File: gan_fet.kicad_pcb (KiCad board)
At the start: 2 copper layers, 10.2 x 22 mm, 7 parts, among them J1 Conn_01x04_Male, Q1 EPC2036, U1 NPC81074

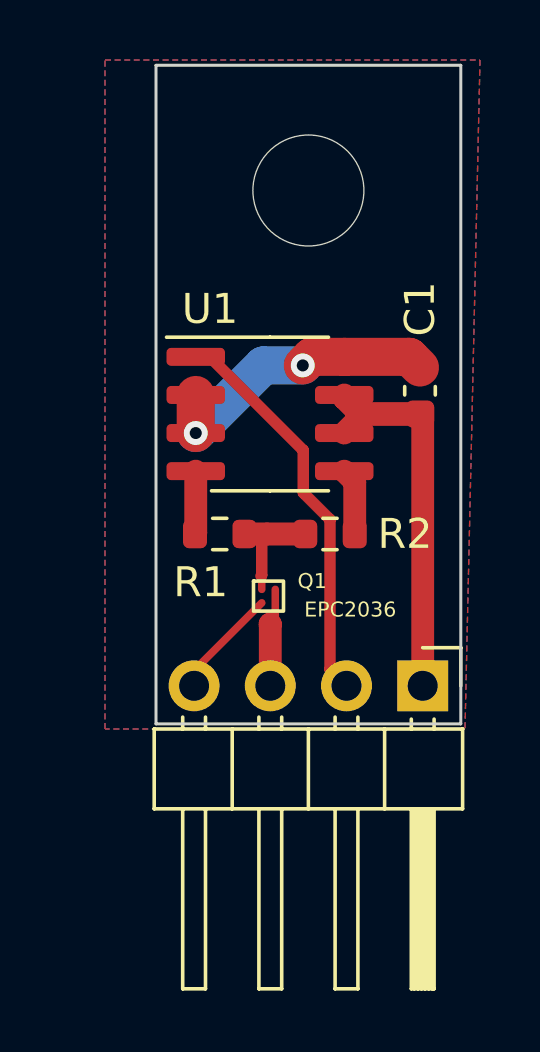
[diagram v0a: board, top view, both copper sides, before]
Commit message: Increased trace width for mosfet drain and source
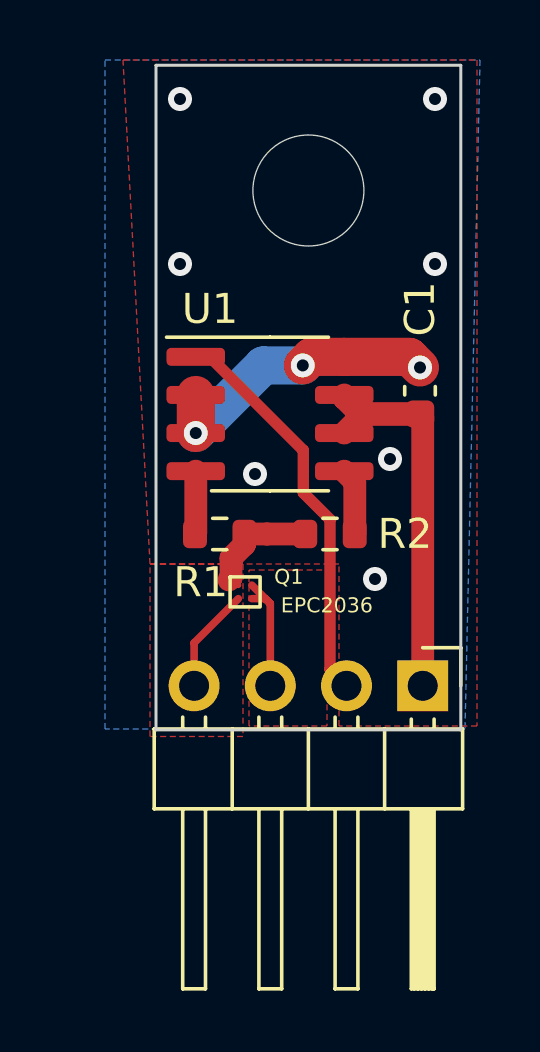
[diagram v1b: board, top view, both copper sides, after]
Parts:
- moved Q1 0.79 mm to (142.2, 96.4)
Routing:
- net /drain: track 3.29 -> 4.29 mm
- net GND: track 13.6 -> 13.5 mm, vias 2 -> 10
- added copper zone on F.Cu, net /drain
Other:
- board size 10.2 x 22 mm -> 10.2 x 22.2 mm
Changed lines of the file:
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@@
   )
   (footprint "epc:epc2036" (layer "F.Cu")
-    (at 143 96.52 90)
+    (at 142.22 96.38 90)
     (property "Sheetfile" "gan_fet.kicad_sch")
     (property "Sheetname" "")
@@
     )
   )
-  (gr_rect (start 149.86 78.375) (end 139.7 100.33) (layer "Edge.Cuts") (width 0.1) (fill none))
+  (gr_rect (start 149.86 78.375) (end 139.7 100.53) (layer "Edge.Cuts") (width 0.1) (fill none))
   (gr_text "+5 G D S" (at 144.999989 97.000009) (layer "B.SilkS")
     (effects (font (size 1.27 1.27) (thickness 0.15)) (justify mirror))
@@
   (segment (start 148.5 90) (end 146.5 90) (width 0.762) (layer "F.Cu") (net 1))
   (segment (start 145.975 89.475) (end 145.975 89.365) (width 0.762) (layer "F.Cu") (net 1))
+  (segment (start 142.445 96.155) (end 140.97 97.63) (width 0.254) (layer "F.Cu") (net 2))
   (segment (start 145.975 88.095) (end 144.877679 88.095) (width 1.27) (layer "F.Cu") (net 2))
+  (segment (start 140.97 97.63) (end 140.97 99.06) (width 0.254) (layer "F.Cu") (net 2))
   (segment (start 148.5 88.45) (end 148.145 88.095) (width 1.27) (layer "F.Cu") (net 2))
   (segment (start 148.145 88.095) (end 145.975 88.095) (width 1.27) (layer "F.Cu") (net 2))
-  (segment (start 143.225 96.295) (end 140.97 98.55) (width 0.254) (layer "F.Cu") (net 2))
   (segment (start 144.877679 88.095) (end 144.59219 88.380489) (width 1.27) (layer "F.Cu") (net 2))
   (segment (start 141.025 90.635) (end 141.025 89.365) (width 1.27) (layer "F.Cu") (net 2))
-  (segment (start 140.97 98.55) (end 140.97 99.06) (width 0.254) (layer "F.Cu") (net 2))
   (via (at 144.59219 88.380489) (size 0.8) (drill 0.4) (layers "F.Cu" "B.Cu") (net 2))
+  (via (at 140.5 79.5) (size 0.8) (drill 0.4) (layers "F.Cu" "B.Cu") (free) (net 2))
+  (via (at 148.5 88.45) (size 0.8) (drill 0.4) (layers "F.Cu" "B.Cu") (net 2))
+  (via (at 149 79.5) (size 0.8) (drill 0.4) (layers "F.Cu" "B.Cu") (free) (net 2))
+  (via (at 147.000011 95.500012) (size 0.8) (drill 0.4) (layers "F.Cu" "B.Cu") (free) (net 2))
+  (via (at 143 92) (size 0.8) (drill 0.4) (layers "F.Cu" "B.Cu") (free) (net 2))
+  (via (at 149 85) (size 0.8) (drill 0.4) (layers "F.Cu" "B.Cu") (free) (net 2))
+  (via (at 140.5 85) (size 0.8) (drill 0.4) (layers "F.Cu" "B.Cu") (free) (net 2))
+  (via (at 147.50001 91.499995) (size 0.8) (drill 0.4) (layers "F.Cu" "B.Cu") (free) (net 2))
   (via (at 141.025 90.635) (size 0.8) (drill 0.4) (layers "F.Cu" "B.Cu") (net 2))
   (segment (start 143.279511 88.380489) (end 141.025 90.635) (width 1.27) (layer "B.Cu") (net 2))
@@
   (segment (start 145.5 98.51) (end 146.05 99.06) (width 0.381) (layer "F.Cu") (net 3))
   (segment (start 145.5 93.515586) (end 145.5 98.51) (width 0.381) (layer "F.Cu") (net 3))
-  (segment (start 143.675 96.825) (end 143.5 97) (width 0.254) (layer "F.Cu") (net 4))
-  (segment (start 143.51 97.01) (end 143.51 99.06) (width 0.762) (layer "F.Cu") (net 4))
-  (segment (start 143.675 95.845) (end 143.675 96.825) (width 0.254) (layer "F.Cu") (net 4))
-  (segment (start 143.5 97) (end 143.51 97.01) (width 0.762) (layer "F.Cu") (net 4))
-  (segment (start 143.225 95.845) (end 143.225 95.425) (width 0.254) (layer "F.Cu") (net 5))
-  (segment (start 143.22442 95.37558) (end 143.22442 94.17558) (width 0.381) (layer "F.Cu") (net 5))
-  (segment (start 143.225 95.425) (end 143.2 95.4) (width 0.254) (layer "F.Cu") (net 5))
-  (segment (start 143.2 95.4) (end 143.22442 95.37558) (width 0.381) (layer "F.Cu") (net 5))
+  (segment (start 143.345 96.155) (end 143.51 96.32) (width 0.254) (layer "F.Cu") (net 4))
+  (segment (start 143.51 96.32) (end 143.51 99.06) (width 0.254) (layer "F.Cu") (net 4))
+  (segment (start 142.895 96.155) (end 143.345 96.155) (width 0.254) (layer "F.Cu") (net 4))
+  (segment (start 142.895 95.705) (end 143.51 96.32) (width 0.254) (layer "F.Cu") (net 4))
+  (segment (start 142.2 95.466732) (end 142.133366 95.533366) (width 0.762) (layer "F.Cu") (net 5))
+  (segment (start 142.65 94) (end 142.65 94.35) (width 0.762) (layer "F.Cu") (net 5))
   (segment (start 144.675 94) (end 143.4 94) (width 0.762) (layer "F.Cu") (net 5))
+  (segment (start 142.65 94.35) (end 142.2 94.8) (width 0.762) (layer "F.Cu") (net 5))
+  (segment (start 142.2 94.8) (end 142.2 95.466732) (width 0.762) (layer "F.Cu") (net 5))
   (segment (start 143.22442 94.17558) (end 143.4 94) (width 0.381) (layer "F.Cu") (net 5))
   (segment (start 143.4 94) (end 142.65 94) (width 0.762) (layer "F.Cu") (net 5))
@@
   (segment (start 145.975 91.905) (end 146.325 92.255) (width 0.762) (layer "F.Cu") (net 7))
   (segment (start 146.325 92.255) (end 146.325 94) (width 0.762) (layer "F.Cu") (net 7))
-  (zone (net 2) (net_name "GND") (layers F&B.Cu) (hatch edge 0.508)
-    (connect_pads (clearance 0.508))
+  (zone (net 2) (net_name "GND") (layer "F.Cu") (hatch edge 0.508)
+    (connect_pads (clearance 0.1524))
+    (min_thickness 0.254) (filled_areas_thickness no)
+    (fill yes (thermal_gap 0.254) (thermal_bridge_width 0.762))
+    (polygon
+      (pts
+        (xy 150.4 100.4)
+        (xy 145.8 100.4)
+        (xy 145.8 95)
+        (xy 139.5 95)
+        (xy 138.6 78.2)
+        (xy 150.4 78.2)
+      )
+    )
+  )
+  (zone (net 4) (net_name "/drain") (layer "F.Cu") (hatch edge 0.508)
+    (connect_pads (clearance 0.1524))
+    (min_thickness 0.254) (filled_areas_thickness no)
+    (fill yes (thermal_gap 0) (thermal_bridge_width 0.508))
+    (polygon
+      (pts
+        (xy 145.4 100.4)
+        (xy 142.8 100.4)
+        (xy 142.8 95.2)
+        (xy 145.4 95.2)
+      )
+    )
+  )
+  (zone (net 2) (net_name "GND") (layer "F.Cu") (hatch edge 0.508)
+    (connect_pads (clearance 0.1524))
+    (min_thickness 0.254) (filled_areas_thickness no)
+    (fill yes (thermal_gap 0) (thermal_bridge_width 0.508))
+    (polygon
+      (pts
+        (xy 142.6 100.75)
+        (xy 139.5 100.75)
+        (xy 139.5 95)
+        (xy 142.6 95)
+      )
+    )
+  )
+  (zone (net 2) (net_name "GND") (layer "B.Cu") (hatch edge 0.508)
+    (connect_pads (clearance 0.1524))
     (min_thickness 0.254) (filled_areas_thickness no)
     (fill yes (thermal_gap 0.508) (thermal_bridge_width 0.508))

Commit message: layout changes
rotate fet 45 degrees
fills/vias for GND and Drain
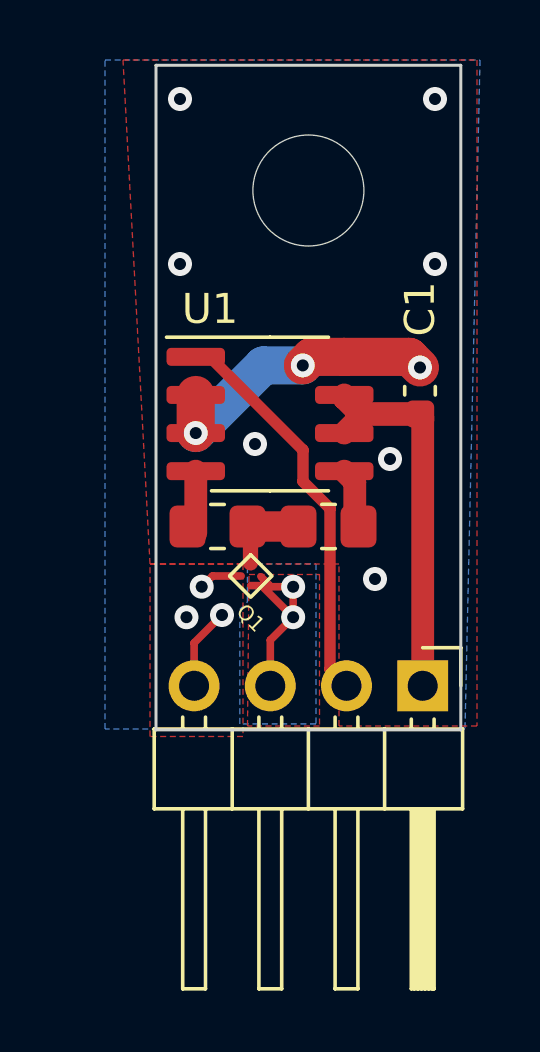
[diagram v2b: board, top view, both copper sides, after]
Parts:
- R1, R2: footprint Resistor_SMD:R_0603_1608Metric -> Resistor_SMD:R_0805_2012Metric_Pad1.20x1.40mm_HandSolder
- moved Q1 0.98 mm to (142.2, 95.4), turned to 45 degrees
- moved R1 0.26 mm to (141.8, 93.8)
- moved R2 0.25 mm to (145.4, 93.8)
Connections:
- net Net-(Q1-Pad3) renamed fetGate
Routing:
- net /drain: track 4.29 -> 6.68 mm, vias 0 -> 2
- net fetGate: track 4.02 -> 3.08 mm
- net GND: track 13.5 -> 14.2 mm, vias 10 -> 13
- added copper zone on B.Cu, net /drain

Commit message: changed pinout, updated EPC footprint
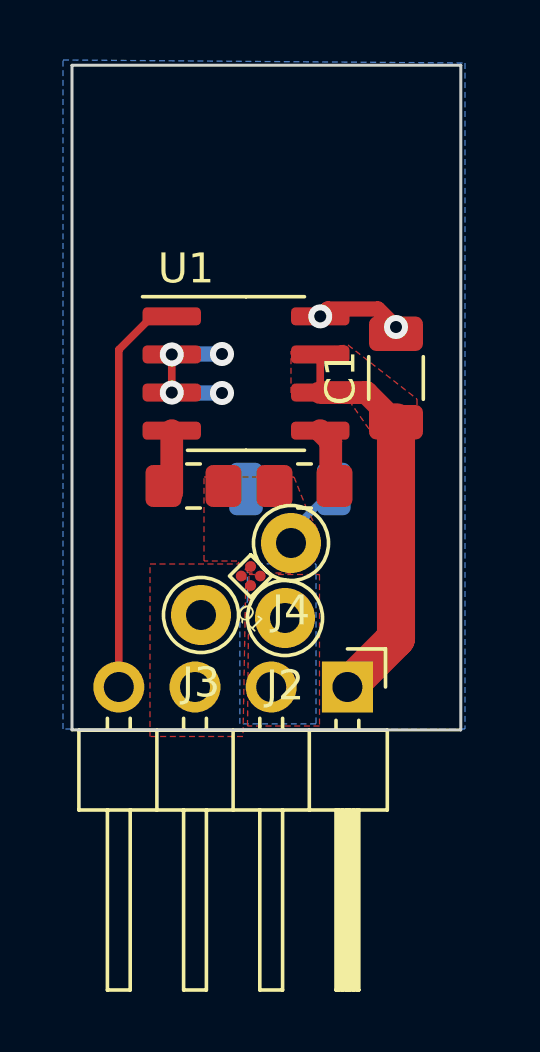
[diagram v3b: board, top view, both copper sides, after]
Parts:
- removed REF**: MountingHole_3.7mm, MountingHole:MountingHole_3.7mm
- added J2: D, Connector_Pin:Pin_D1.0mm_L10.0mm, F.Cu at (144.0, 96.8)
- added J3: S, Connector_Pin:Pin_D1.0mm_L10.0mm, F.Cu at (141.2, 96.7)
- added J4: G, Connector_Pin:Pin_D1.0mm_L10.0mm, F.Cu at (144.2, 94.3)
- added TP1: C_Small, Resistor_SMD:R_1206_3216Metric, B.Cu at (144.2, 92.5)
- C1: footprint Capacitor_SMD:C_0603_1608Metric -> Capacitor_SMD:C_1206_3216Metric
- moved J1 2.51 mm to (146.1, 99.1)
- moved R1 1.57 mm to (140.9, 92.4)
- moved U1 1.57 mm to (142.7, 88.7)
- moved R2 1.57 mm to (144.7, 92.4)
- moved C1 0.91 mm to (147.7, 88.8)
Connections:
- net fetGate renamed /fetGate
- J1 pad 2: /gate -> /drain
- J1 pad 3: /drain -> GND
- J1 pad 4: GND -> /gate
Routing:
- net /drain: track 6.68 -> 0.00 mm, vias 2 -> 0
- net GND: track 14.2 -> 7.51 mm, vias 13 -> 6
- net /fetGate: track 3.08 -> 2.39 mm
- added copper zone on F.Cu, net +5V
- added copper zone on F.Cu, net /fetGate
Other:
- board size 10.2 x 22.2 mm -> 13 x 22.2 mm

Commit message: FET to backside, added PTH for BS170 pinout now matches IRF510 better EPC2036 footprint (pad and mask)
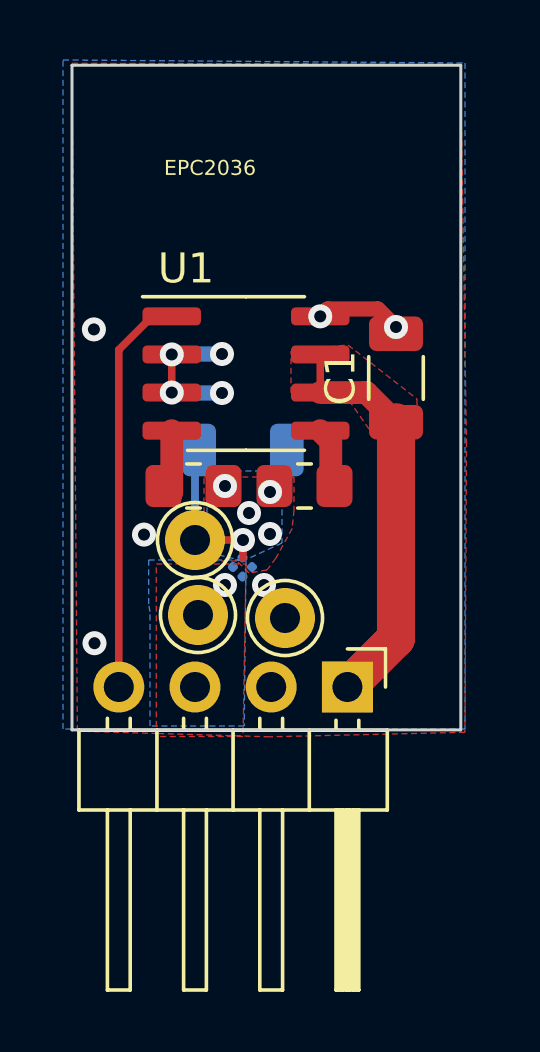
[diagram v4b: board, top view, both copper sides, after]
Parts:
- Q1: moved to B.Cu
- moved J4 3.20 mm to (141.0, 94.2)
- moved TP1 2.03 mm to (142.6, 91.2), turned to 0 degrees
- moved Q1 1.04 mm to (143.2, 95.1), turned to 135 degrees
- moved J3 0.10 mm to (141.1, 96.7)
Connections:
- J1 pad 2: /drain -> GND
- J1 pad 3: GND -> /drain
- J2 pad 1: /drain -> GND
- J3 pad 1: GND -> /drain
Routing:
- net /fetGate: track 2.39 -> 5.86 mm, vias 0 -> 5
- net GND: vias 6 -> 10
- net /drain: vias 0 -> 1
- added copper zone on B.Cu, net /fetGate
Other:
- board text added: "+5 S D G"
- board text removed: "+5 G D S"

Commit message: Rev0 board to JLCPCB
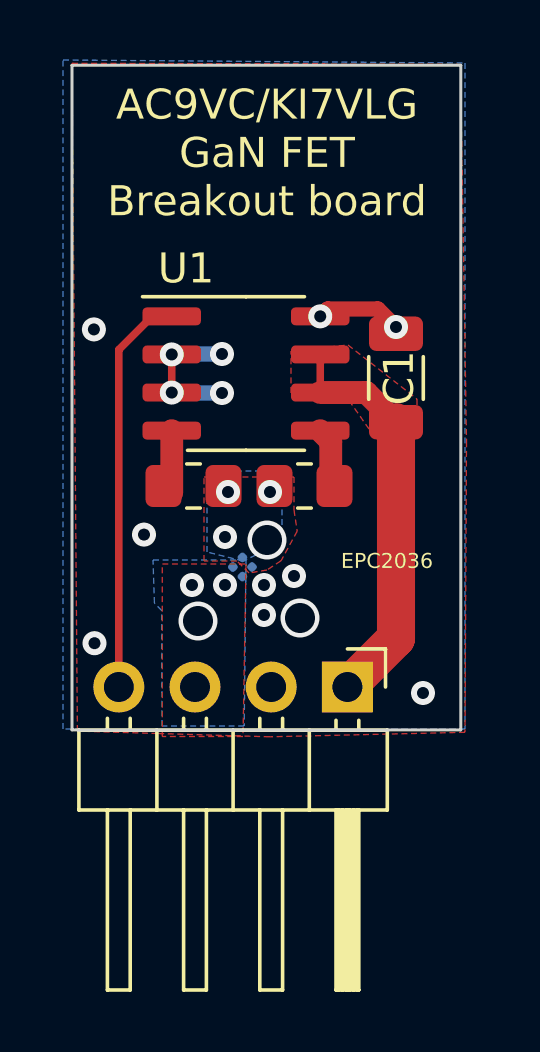
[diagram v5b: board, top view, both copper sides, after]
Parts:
- removed J2: D, Connector_Pin:Pin_D1.0mm_L10.0mm
- removed J3: S, Connector_Pin:Pin_D1.0mm_L10.0mm
- removed J4: G, Connector_Pin:Pin_D1.0mm_L10.0mm
- removed TP1: C_Small, Resistor_SMD:R_1206_3216Metric
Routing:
- net /fetGate: track 5.86 -> 0.00 mm, vias 5 -> 4
- net +5V: track 14.7 -> 14.0 mm
- net GND: vias 10 -> 14
- net /drain: vias 1 -> 3
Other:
- rule pad_to_mask_clearance: 0.000051 -> 0
- board text added: "AC9VC/KI7VLG GaN FET Breakout board"
